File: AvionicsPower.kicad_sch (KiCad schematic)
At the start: 15 parts, among them Q1 AO3400A, U1 TLV62585RWTR, U2 TPS77533PWPR

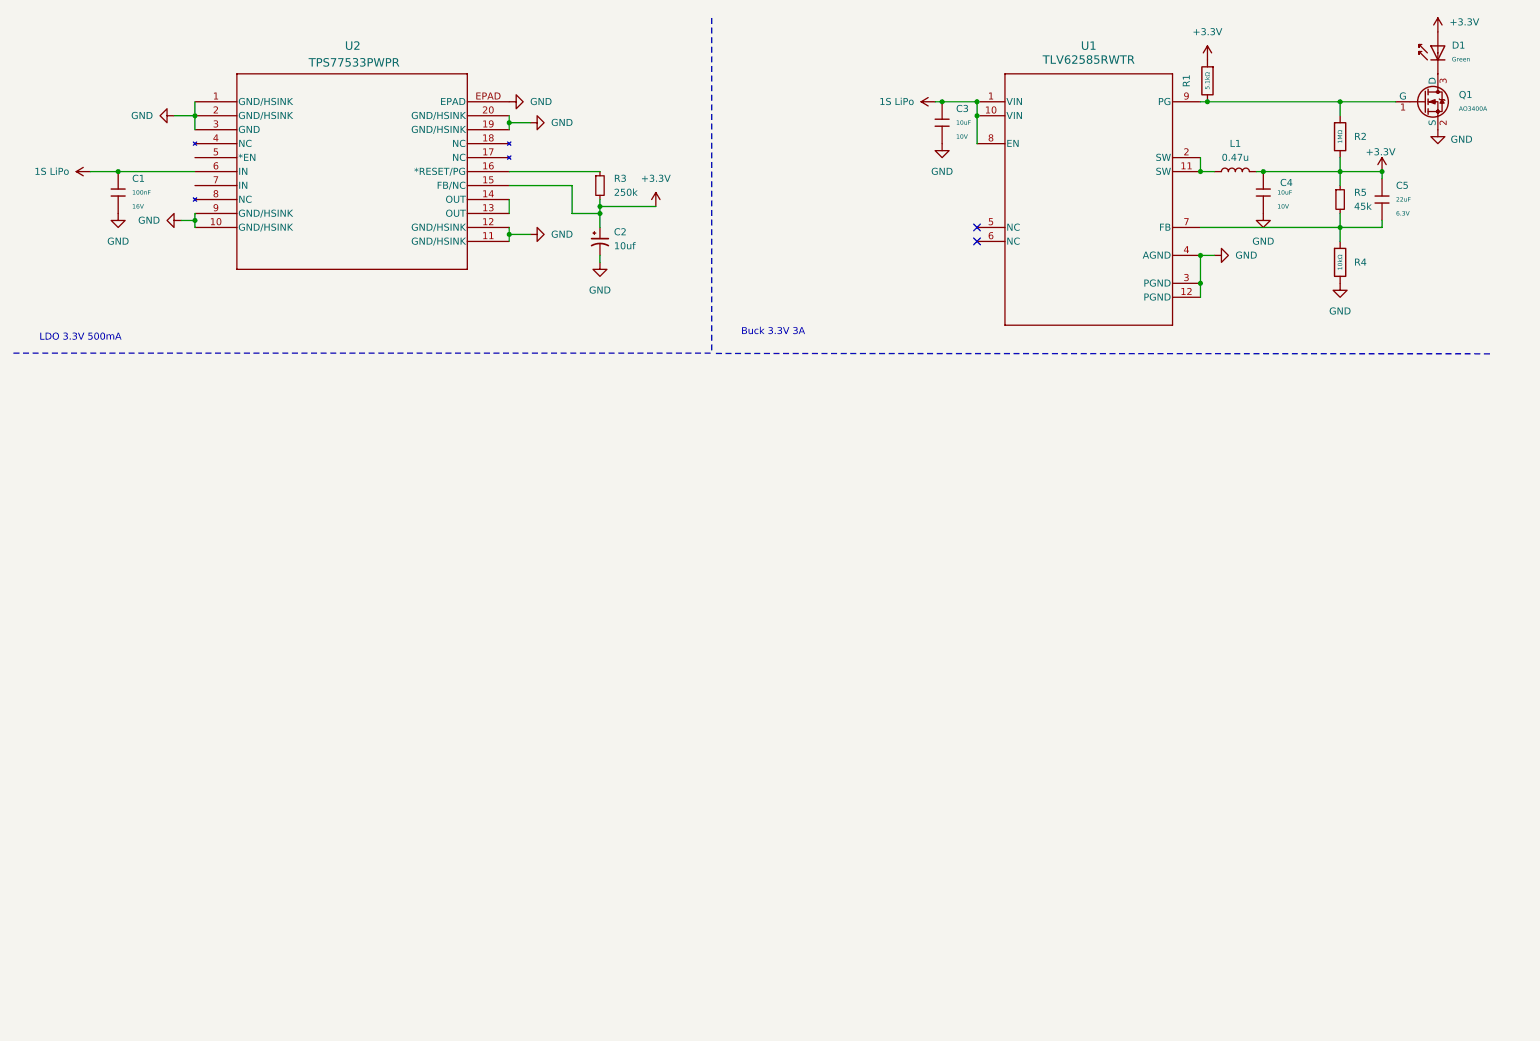
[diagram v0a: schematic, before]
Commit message: Added USB-C Connector, Added LDO, Added RP2040, Added Debug LEDs
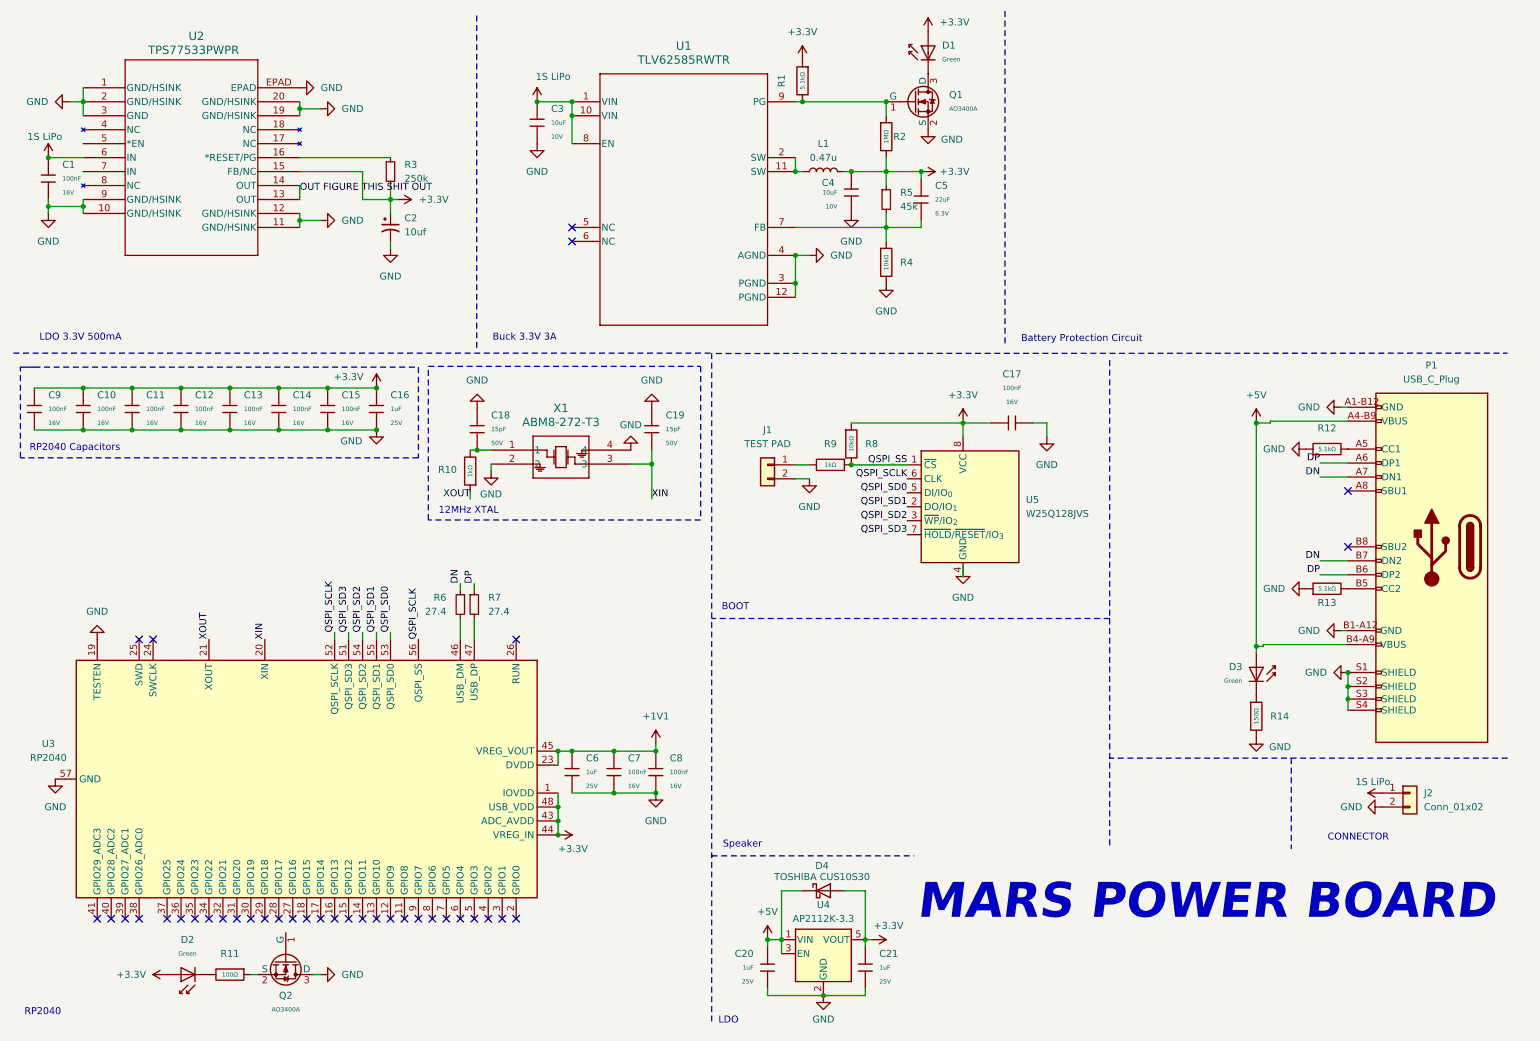
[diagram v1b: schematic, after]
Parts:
- added C10, C11, C12, C13, C14, C15, C17, C7, C8, C9: 100nF, PCM_JLCPCB:C_0402, symbol PCM_JLCPCB-Capacitors:0402,100nF
- added C16, C20, C21, C6: 1uF, PCM_JLCPCB:C_0402, symbol PCM_JLCPCB-Capacitors:0402,1uF
- added C18, C19: 15pF, PCM_JLCPCB:C_0402, symbol PCM_JLCPCB-Capacitors:0402,15pF
- added D2, D3: Green, PCM_JLCPCB:D_0805, symbol PCM_JLCPCB-Diodes:LED,0805,Green
- added D4: TOSHIBA CUS10S30, PCM_JLCPCB:D_SOD-323, symbol Device:D_Schottky
- added J1: TEST PAD, symbol Connector_Generic:Conn_01x02
- added J2: Conn_01x02, symbol Connector_Generic:Conn_01x02
- added P1: USB_C_Plug, symbol MC-311D:USB_C_Plug_12pin
- added Q2: AO3400A, PCM_JLCPCB:Q_SOT-23, symbol PCM_JLCPCB-Transistors:NMOS,AO3400A
- added R10, R9: 1kΩ, PCM_JLCPCB:R_0402, symbol PCM_JLCPCB-Resistors:0402,1kΩ
- added R11: 100Ω, PCM_JLCPCB:R_0402, symbol PCM_JLCPCB-Resistors:0402,100Ω
- added R12, R13: 5.1kΩ, PCM_JLCPCB:R_0402, symbol PCM_JLCPCB-Resistors:0402,5.1kΩ
- added R14: 150Ω, PCM_JLCPCB:R_0805, symbol PCM_JLCPCB-Resistors:0805,150Ω
- added R6, R7: 27.4, Capacitor_SMD:C_0402_1005Metric, symbol Device:R_Small
- added R8: 10kΩ, PCM_JLCPCB:R_0402, symbol PCM_JLCPCB-Resistors:0402,10kΩ
- added U3: RP2040, Package_DFN_QFN:QFN-56-1EP_7x7mm_P0.4mm_EP3.2x3.2mm, symbol MCU_RaspberryPi:RP2040
- added U4: AP2112K-3.3, Package_TO_SOT_SMD:SOT-23-5, symbol Regulator_Linear:AP2112K-3.3
- added U5: W25Q128JVS, Package_SO:SOIC-8_5.3x5.3mm_P1.27mm, symbol Memory_Flash:W25Q128JVS
- added X1: ABM8-272-T3, ABM8-272-T3_ABR, symbol ABM8_272_T3:ABM8-272-T3
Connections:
- net +3.3V: now also C10.1, C11.1, C12.1, C13.1, C14.1, C15.1, C16.1, C17.1, C21.1, C9.1, D2.2, D4.2 (A), R8.1, U3.1 (IOVDD), U3.10 (IOVDD), U3.22 (IOVDD), U3.33 (IOVDD), U3.42 (IOVDD), U3.43 (ADC_AVDD), U3.44 (VREG_IN), U3.48 (USB_VDD), U3.49 (IOVDD), U4.5 (VOUT), U5.8 (VCC)
- net 1S LiPo: now also J2.1 (Pin_1)
- net GND: now also C10.2, C11.2, C12.2, C13.2, C14.2, C15.2, C16.2, C17.2, C18.1, C19.1, C20.1, C21.2, C6.2, C7.2, C8.2, C9.2, J1.2 (Pin_2), J2.2 (Pin_2), P1.A1-B12 (GND), P1.B1-A12 (GND), P1.S1 (SHIELD), P1.S2 (SHIELD), P1.S3 (SHIELD), P1.S4 (SHIELD), Q2.3 (D), R12.1, R13.1, R14.2, U3.19 (TESTEN), U3.57 (GND), U4.2 (GND), U5.4 (GND), X1.2, X1.4
- net OUT FIGURE THIS SHIT OUT: now reaches U2.13 (OUT), U2.14 (OUT)
- new net: P1.B5 (CC2), R13.2
- new net: D2.1, R11.2
- new net: Q2.2 (S), R11.1
- new net: R6.2, U3.46 (USB_DM)
- new net: R7.2, U3.47 (USB_DP)
- new net: D3.1, R14.1
- new net: J1.1 (Pin_1), R9.2
- new net: C18.2, R10.2, X1.1
- new net: P1.A5 (CC1), R12.2
- new net +1V1: C6.1, C7.1, C8.1, U3.23 (DVDD), U3.45 (VREG_VOUT), U3.50 (DVDD)
- new net +5V: C20.2, D3.2, D4.1 (K), P1.A4-B9 (VBUS), P1.B4-A9 (VBUS), U4.1 (VIN), U4.3 (EN)
- new net DN: P1.A7 (DN1), P1.B7 (DN2), R6.1
- new net DP: P1.A6 (DP1), P1.B6 (DP2), R7.1
- new net QSPI_SCLK: U3.52 (QSPI_SCLK), U3.56 (QSPI_SS), U5.6 (CLK)
- new net QSPI_SD0: U3.53 (QSPI_SD0), U5.5 (DI/IO_{0})
- new net QSPI_SD1: U3.55 (QSPI_SD1), U5.2 (DO/IO_{1})
- new net QSPI_SD2: U3.54 (QSPI_SD2), U5.3 (~{WP}/IO_{2})
- new net QSPI_SD3: U3.51 (QSPI_SD3), U5.7 (~{HOLD}/~{RESET}/IO_{3})
- new net QSPI_SS: R8.2, R9.1, U5.1 (~{CS})
- new net XIN: C19.2, U3.20 (XIN), X1.3
- new net XOUT: R10.1, U3.21 (XOUT)
- no-connect marks 2 -> 37
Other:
- note added: "12MHz XTAL"
- note added: "BOOT"
- note added: "Battery Protection Circuit"
- note added: "CONNECTOR"
- note added: "LDO"
- note added: "MARS POWER BOARD"
- note added: "RP2040"
- note added: "RP2040 Capacitors"
- note added: "Speaker"
- moved on the sheet: C1, C2, C3, C4, C5, D1, L1, Q1, R1, R2, R3, R4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

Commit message: Added Battery Management IC
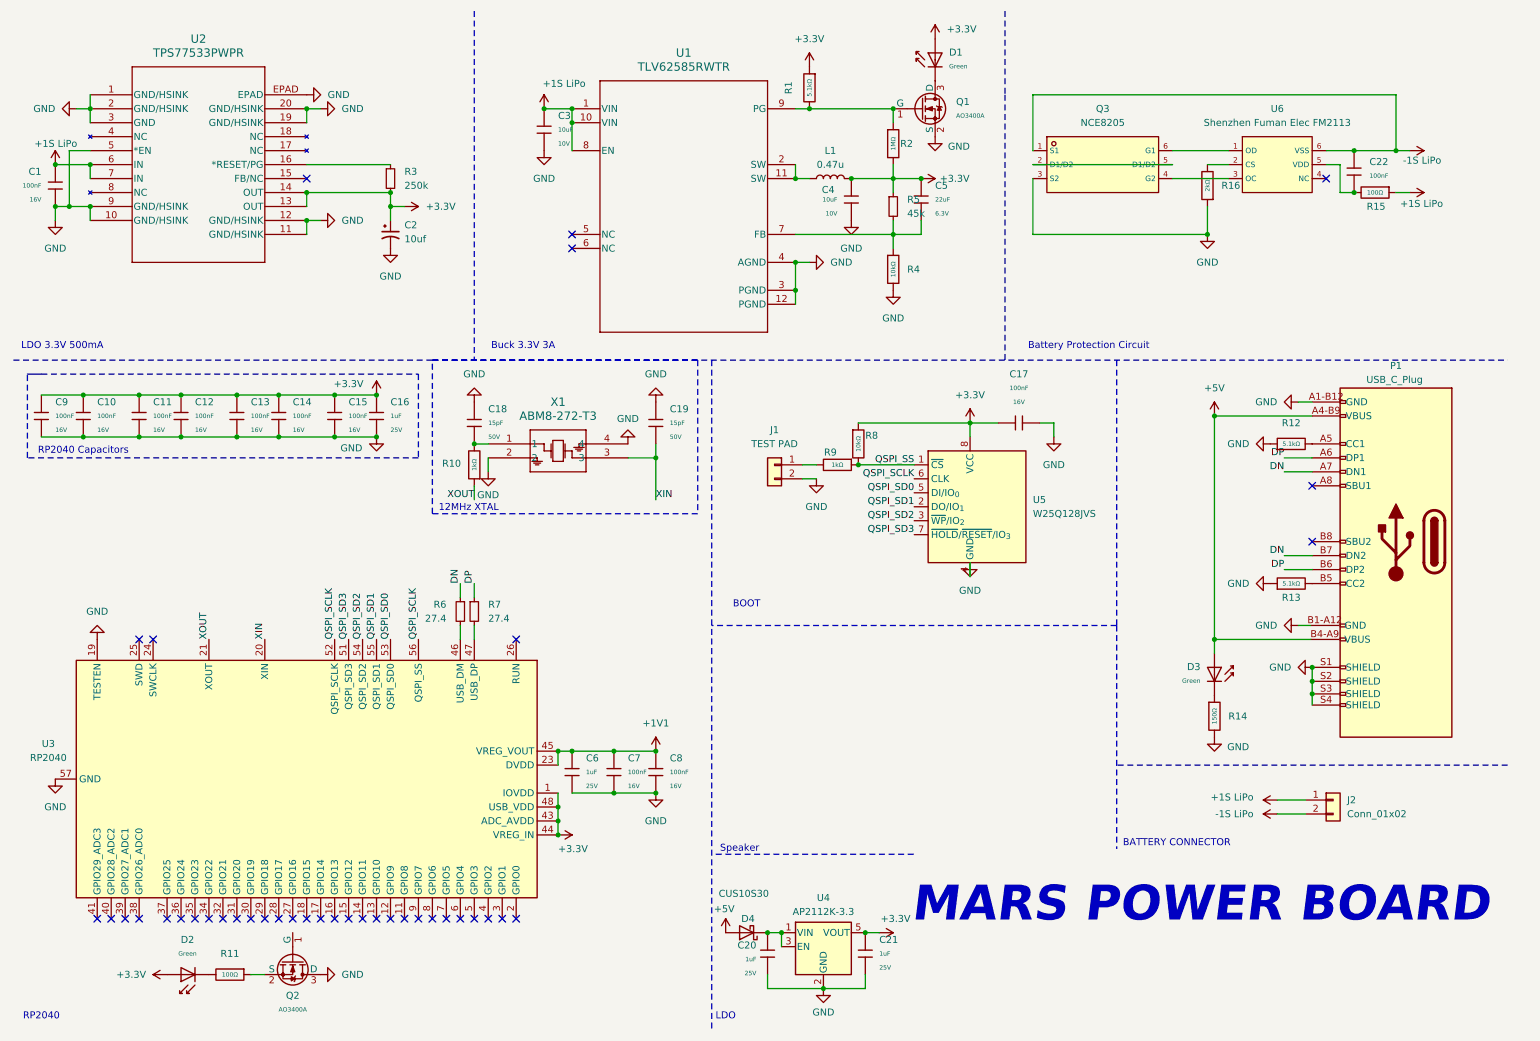
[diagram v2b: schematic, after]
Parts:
- added C22: 100nF, PCM_JLCPCB:C_0402, symbol PCM_JLCPCB-Capacitors:0402,100nF
- added Q3: NCE8205, PCM_JLCPCB:SOT-23-6_L2.9-W1.6-P0.95-LS2.8-BR, symbol PCM_JLCPCB-Transistor-Packages:NMOS, 2 Channel, HJ8205
- added R15: 100Ω, PCM_JLCPCB:R_0402, symbol PCM_JLCPCB-Resistors:0402,100Ω
- added R16: 2kΩ, PCM_JLCPCB:R_0402, symbol PCM_JLCPCB-Resistors:0402,2kΩ
- added U6: Shenzhen Fuman Elec FM2113, PCM_JLCPCB:SOT-23-6_L2.9-W1.6-P0.95-LS2.8-BL, symbol PCM_JLCPCB-Power:Battery, Li-Ion, 0.5A, TP4057
- D4: value TOSHIBA CUS10S30 -> CUS10S30
- J2: LCSC (none) -> C131337
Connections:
- net 1S LiPo is gone; now on net +1S LiPo: C1.1, C3.1, J2.1 (Pin_1), U1.1 (VIN), U1.10 (VIN), U1.8 (EN), U2.6 (IN)
- net OUT FIGURE THIS SHIT OUT is gone; now on net +3.3V: U2.13 (OUT), U2.14 (OUT)
- net +3.3V: no longer D4.2 (A), U2.15 (FB/NC)
- net +5V: now also D4.2 (A); no longer C20.2, D4.1 (K), U4.1 (VIN), U4.3 (EN)
- net GND: now also U2.5 (*EN), Q3.3 (S2), R16.1; no longer J2.2 (Pin_2)
- net +1S LiPo: now reaches U2.7 (IN)
- net +1S LiPo: now also R15.1
- new net: C22.2, R15.2, U6.5 (VDD)
- new net: R16.2, U6.2 (CS)
- new net: C20.2, D4.1 (K), U4.1 (VIN), U4.3 (EN)
- new net: Q3.2 (D1/D2), Q3.5 (D1/D2)
- new net: Q3.4 (G2), U6.3 (OC)
- new net: Q3.6 (G1), U6.1 (OD)
- new net -1S LiPo: C22.1, J2.2 (Pin_2), Q3.1 (S1), U6.6 (VSS)
- no-connect marks 37 -> 39
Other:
- note added: "BATTERY CONNECTOR"
- note removed: "CONNECTOR"
- moved on the sheet: C1, C10, C11, C12, C13, C14, C15, C16, C17, C18, C19, C2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

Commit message: Added Class D Amplifier and Speaker
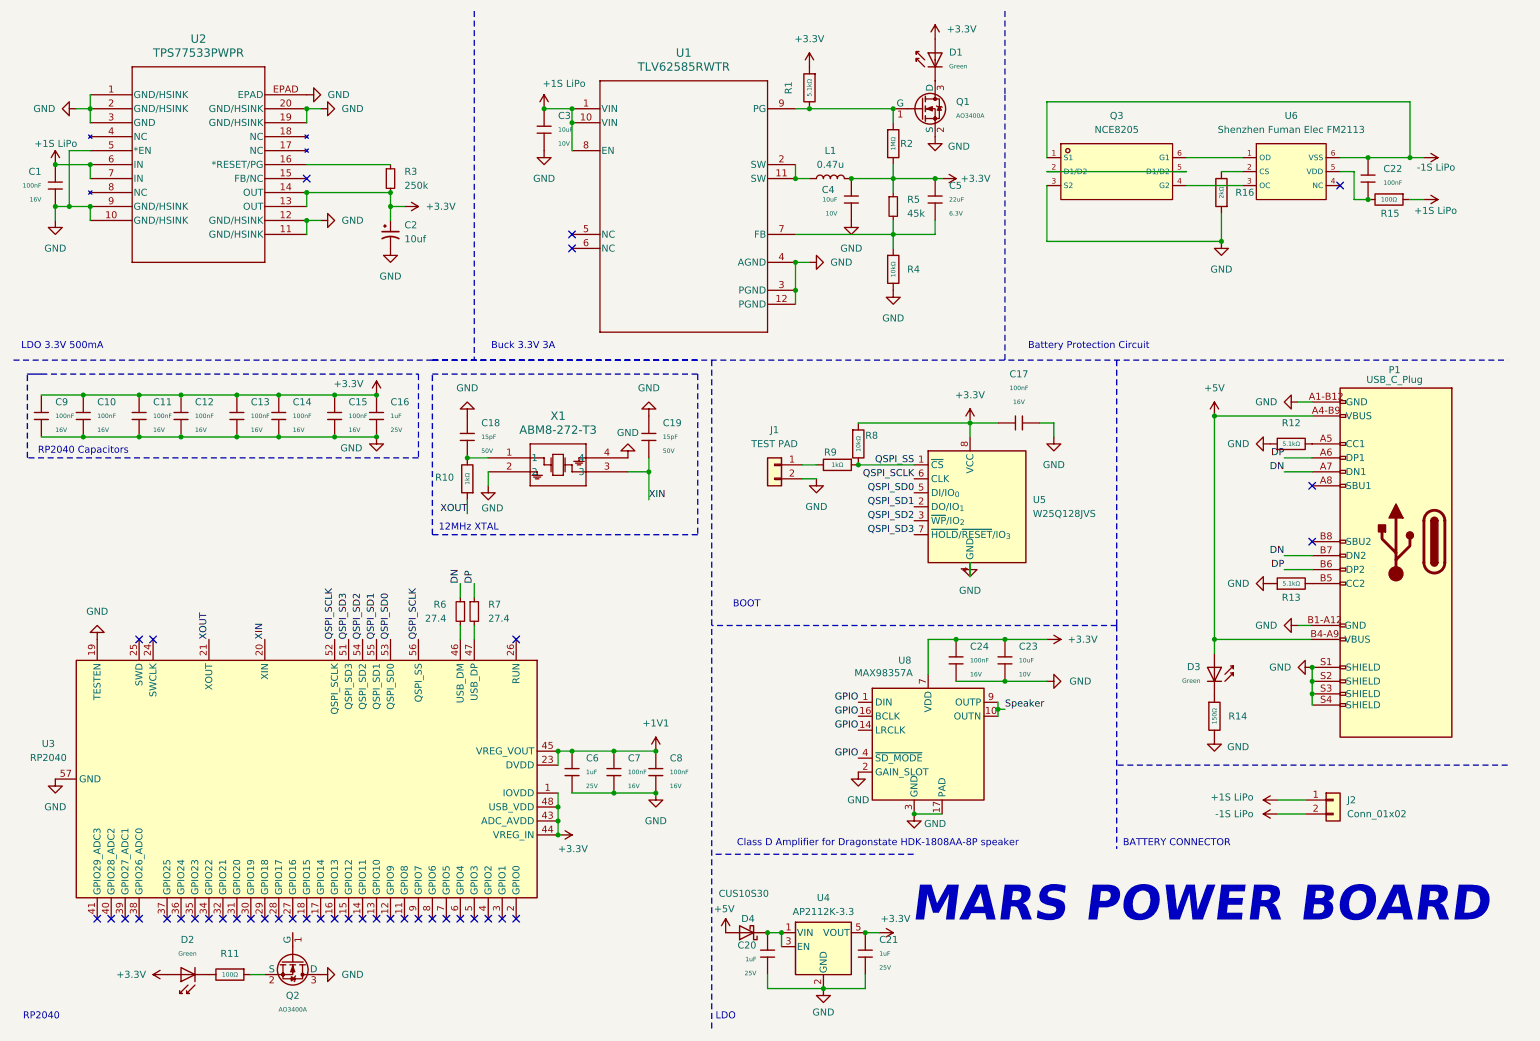
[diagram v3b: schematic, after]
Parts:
- added C23: 10uF, PCM_JLCPCB:C_0603, symbol PCM_JLCPCB-Capacitors:0603,10uF
- added C24: 100nF, PCM_JLCPCB:C_0402, symbol PCM_JLCPCB-Capacitors:0402,100nF
- added U8: MAX98357A, Package_DFN_QFN:TQFN-16-1EP_3x3mm_P0.5mm_EP1.23x1.23mm, symbol Audio:MAX98357A
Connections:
- net +3.3V: now also C23.1, C24.1, U8.7 (VDD), U8.8 (VDD)
- net GND: now also C23.2, C24.2, U8.11 (GND), U8.15 (GND), U8.17 (PAD), U8.2 (GAIN_SLOT), U8.3 (GND)
- new net GPIO: U8.1 (DIN), U8.14 (LRCLK), U8.16 (BCLK), U8.4 (~{SD_MODE})
- new net Speaker: U8.10 (OUTN), U8.9 (OUTP)
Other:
- note added: "Class D Amplifier for Dragonstate HDK-1808AA-8P speaker"
- note removed: "Speaker"
- moved on the sheet: C18, C19, C22, C5, Q3, R10, R15, R16, U6, X1
